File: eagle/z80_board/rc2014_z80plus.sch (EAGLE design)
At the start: 15 parts, among them IC1 74HCT14N, IC2 Z80

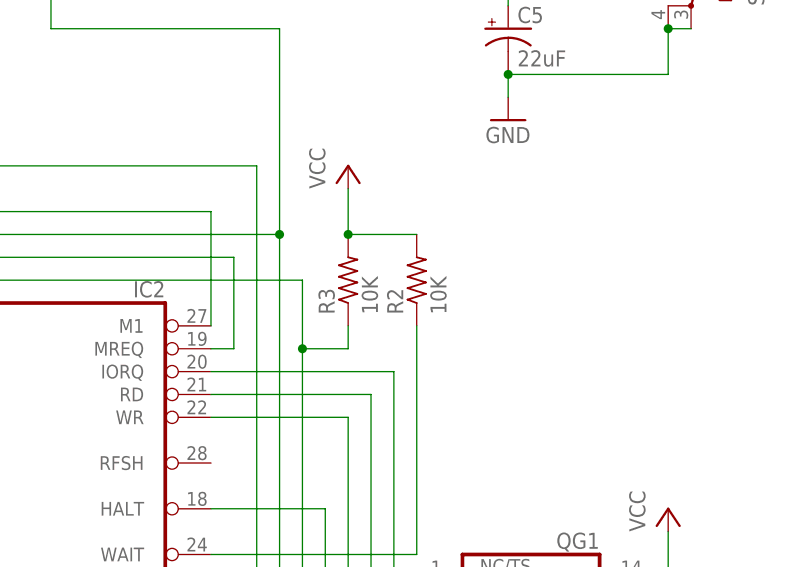
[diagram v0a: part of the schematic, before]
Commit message: Update resistor values
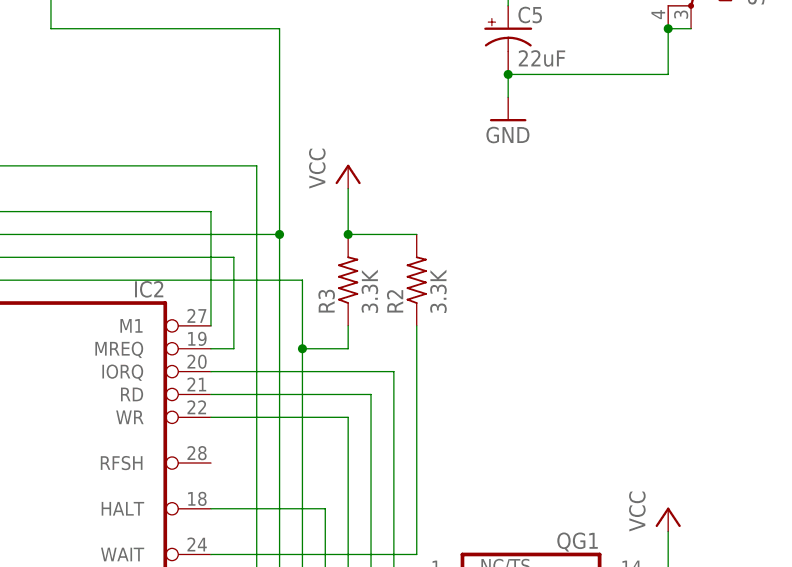
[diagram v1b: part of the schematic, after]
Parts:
- R2, R3: value 10K -> 3.3K
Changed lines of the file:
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@@
 <?xml version="1.0" encoding="utf-8"?>
 <!DOCTYPE eagle SYSTEM "eagle.dtd">
-<eagle version="8.1.0">
+<eagle version="8.1.1">
 <drawing>
 <settings>
@@
 <part name="D1" library="diode" deviceset="1N4148" device="DO35-10"/>
 <part name="R1" library="rcl" deviceset="R-US_" device="0207/10" value="10K"/>
-<part name="R2" library="rcl" deviceset="R-US_" device="0207/10" value="10K"/>
+<part name="R2" library="rcl" deviceset="R-US_" device="0207/10" value="3.3K"/>
 <part name="GND1" library="supply1" deviceset="GND" device=""/>
 <part name="P+4" library="supply1" deviceset="VCC" device=""/>
 <part name="IC1" library="74xx-eu" deviceset="74*14" device="N" technology="HCT"/>
-<part name="R3" library="rcl" deviceset="R-US_" device="0207/10" value="10K"/>
+<part name="R3" library="rcl" deviceset="R-US_" device="0207/10" value="3.3K"/>
 <part name="P+5" library="supply1" deviceset="VCC" device=""/>
 <part name="GND5" library="supply1" deviceset="GND" device=""/>
